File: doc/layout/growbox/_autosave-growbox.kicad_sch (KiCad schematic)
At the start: 12 parts

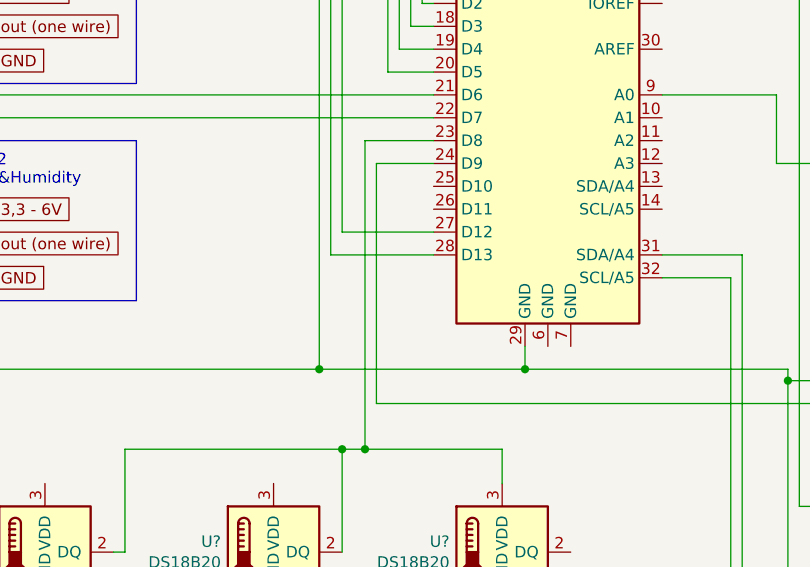
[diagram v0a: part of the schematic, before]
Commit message: -Schaltplan update (DHT22, Heizung) -Schaltplan korrektur (SHELLY DS18B20 auf OneWire DP8) -Interrupt Timer1 auf Timer2 geändert 	-SoftwareSerial wird von Timer1 beeinflusst und damit disfunktional 	-PIN dazu von D9 auf D11 geändert -Up and running again during grow
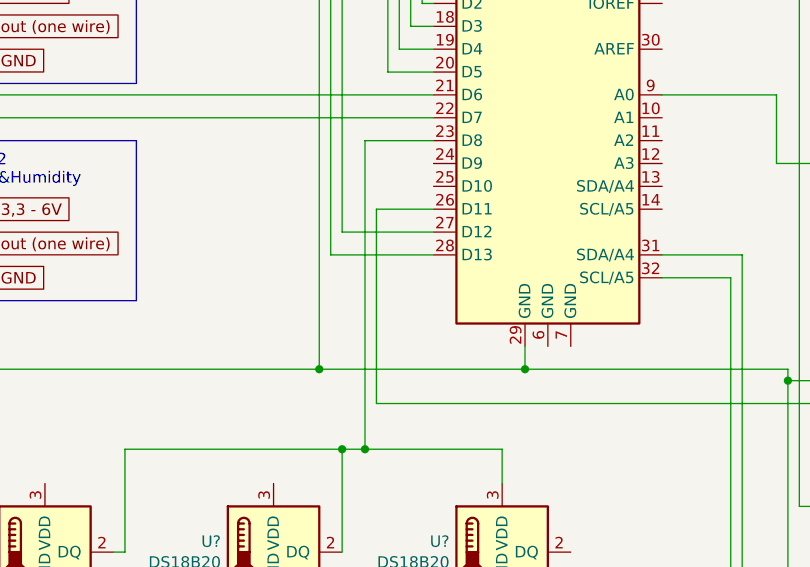
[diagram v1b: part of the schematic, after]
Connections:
- net PWM_in: now also A?.26 (D11); no longer A?.24 (D9)
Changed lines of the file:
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@@
+    (stroke (width 0) (type default))
+  )
+  (wire (pts (xy 74.93 107.95) (xy 81.28 107.95))
     (stroke (width 0) (type default))
   )
@@
     (stroke (width 0) (type default))
   )
-  (wire (pts (xy 74.93 129.54) (xy 74.93 102.87))
+  (wire (pts (xy 74.93 129.54) (xy 74.93 107.95))
     (stroke (width 0) (type default))
   )
@@
     (stroke (width 0) (type default))
   )
-  (wire (pts (xy 74.93 102.87) (xy 81.28 102.87))
-    (stroke (width 0) (type default))
-  )
